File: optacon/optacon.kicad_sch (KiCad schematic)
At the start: 5 parts

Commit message: driver board
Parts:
- added C5: 0.1µF, Capacitor_SMD:C_1206_3216Metric, symbol Device:C
- added R7: 0R, Resistor_SMD:R_1206_3216Metric, symbol Device:R
- added R8: DNP, Resistor_SMD:R_1206_3216Metric, symbol Device:R
- D1: value (none) -> D; footprint (none) -> Diode_SMD:D_SOD-123F
- J1: value (none) -> Conn_01x12; footprint (none) -> microchip_hv:FH34SRJ-12S-0.5SH
- U1, U2: value (none) -> HV528; footprint (none) -> Package_DFN_QFN:HVQFN-32-1EP_5x5mm_P0.5mm_EP3.1x3.1mm
- piezo1: value (none) -> Conn_01x21; footprint (none) -> microchip_hv:piezox20
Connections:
- net AIN: now also J1.2 (Pin_2); no longer J1.11 (Pin_11)
- net CLK: now also J1.10 (Pin_10); no longer J1.4 (Pin_4)
- net DIN: now also J1.11 (Pin_11), U2.17 (DIN); no longer J1.3 (Pin_3), U1.17 (DIN)
- net DOUT: now also U1.24 (DOUT); no longer U2.24 (DOUT)
- net GND: now also J1.1 (Pin_1), C5.1; no longer J1.12 (Pin_12)
- net LE: now also J1.8 (Pin_8); no longer J1.6 (Pin_6)
- net POL: now also J1.9 (Pin_9); no longer J1.5 (Pin_5)
- net REG: now also J1.3 (Pin_3); no longer J1.10 (Pin_10)
- net SCL: now also J1.5 (Pin_5); no longer J1.8 (Pin_8)
- net SDA: now also J1.4 (Pin_4); no longer J1.9 (Pin_9)
- net VBIAS: now also J1.6 (Pin_6); no longer J1.2 (Pin_2)
- net VDD: now also J1.12 (Pin_12); no longer J1.1 (Pin_1)
- net VPP: now also C5.2, R7.2, R8.2
- new net: U1.17 (DIN), U2.24 (DOUT)
- new net VBST: R8.1
- new net VOUT: R7.1
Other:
- sheet hv_driver ports: added VBST; removed none
- moved on the sheet: J1

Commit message: cleanup
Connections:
- net AIN: now also J1.8 (Pin_8); no longer J1.2 (Pin_2)
- net CLK: now also J1.6 (Pin_6); no longer J1.10 (Pin_10)
- net DIN: now also J1.7 (Pin_7); no longer J1.11 (Pin_11)
- net DOUT: now also J1.3 (Pin_3); no longer J1.7 (Pin_7)
- net LE: now also J1.4 (Pin_4); no longer J1.8 (Pin_8)
- net POL: now also J1.5 (Pin_5); no longer J1.9 (Pin_9)
- net REG: now also J1.11 (Pin_11); no longer J1.3 (Pin_3)
- net SCL: now also J1.9 (Pin_9); no longer J1.5 (Pin_5)
- net SDA: now also J1.10 (Pin_10); no longer J1.4 (Pin_4)
- net VBIAS: now also J1.2 (Pin_2); no longer J1.6 (Pin_6)
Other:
- moved on the sheet: R7, R8
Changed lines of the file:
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@@
   (junction (at 167.64 43.18) (diameter 0) (color 0 0 0 0)
   )
+  (junction (at 111.76 92.71) (diameter 0) (color 0 0 0 0)
+  )
   (junction (at 214.63 113.03) (diameter 0) (color 0 0 0 0)
   )
@@
   )
   (junction (at 214.63 66.04) (diameter 0) (color 0 0 0 0)
-  )
-  (junction (at 111.76 92.71) (diameter 0) (color 0 0 0 0)
   )
   (junction (at 214.63 68.58) (diameter 0) (color 0 0 0 0)
@@
     (stroke (width 0) (type default) (color 0 0 0 0))
   )
-  (wire (pts (xy 104.14 97.79) (xy 104.14 99.06))
-    (stroke (width 0) (type default) (color 0 0 0 0))
-  )
   (wire (pts (xy 214.63 110.49) (xy 214.63 111.76))
     (stroke (width 0) (type default) (color 0 0 0 0))
@@
     (stroke (width 0) (type default) (color 0 0 0 0))
   )
+  (wire (pts (xy 54.61 91.44) (xy 59.69 91.44))
+    (stroke (width 0) (type default) (color 0 0 0 0))
+  )
   (wire (pts (xy 210.82 115.57) (xy 214.63 115.57))
     (stroke (width 0) (type default) (color 0 0 0 0))
@@
     (stroke (width 0) (type default) (color 0 0 0 0))
   )
-  (wire (pts (xy 111.76 92.71) (xy 111.76 99.06))
+  (wire (pts (xy 111.76 92.71) (xy 111.76 97.79))
     (stroke (width 0) (type default) (color 0 0 0 0))
   )
@@
     (stroke (width 0) (type default) (color 0 0 0 0))
   )
+  (wire (pts (xy 111.76 87.63) (xy 111.76 92.71))
+    (stroke (width 0) (type default) (color 0 0 0 0))
+  )
   (wire (pts (xy 210.82 73.66) (xy 214.63 73.66))
     (stroke (width 0) (type default) (color 0 0 0 0))
@@
     (stroke (width 0) (type default) (color 0 0 0 0))
   )
-  (wire (pts (xy 104.14 87.63) (xy 104.14 92.71))
-    (stroke (width 0) (type default) (color 0 0 0 0))
-  )
   (wire (pts (xy 168.91 40.64) (xy 168.91 107.95))
     (stroke (width 0) (type default) (color 0 0 0 0))
@@
     (effects (font (size 1.27 1.27)) (justify right bottom))
   )
-  (label "AIN" (at 27.94 66.04 0)
+  (label "AIN" (at 27.94 50.8 0)
     (effects (font (size 1.27 1.27)) (justify left bottom))
   )
@@
     (effects (font (size 1.27 1.27)) (justify right bottom))
   )
-  (label "DOUT" (at 27.94 53.34 0)
+  (label "DOUT" (at 27.94 63.5 0)
     (effects (font (size 1.27 1.27)) (justify left bottom))
   )
@@
     (effects (font (size 1.27 1.27)) (justify left bottom))
   )
-  (label "SDA" (at 27.94 60.96 0)
+  (label "SDA" (at 27.94 45.72 0)
     (effects (font (size 1.27 1.27)) (justify left bottom))
   )
@@
     (effects (font (size 1.27 1.27)) (justify left bottom))
   )
-  (label "DIN" (at 27.94 43.18 0)
+  (label "DIN" (at 27.94 53.34 0)
     (effects (font (size 1.27 1.27)) (justify left bottom))
   )
@@
     (effects (font (size 1.27 1.27)) (justify left bottom))
   )
-  (label "POL" (at 27.94 48.26 0)
+  (label "POL" (at 27.94 58.42 0)
     (effects (font (size 1.27 1.27)) (justify left bottom))
   )
@@
     (effects (font (size 1.27 1.27)) (justify left bottom))
   )
-  (label "LE" (at 27.94 50.8 0)
+  (label "LE" (at 27.94 60.96 0)
     (effects (font (size 1.27 1.27)) (justify left bottom))
   )
@@
     (effects (font (size 1.27 1.27)) (justify left bottom))
   )
-  (label "VBIAS" (at 27.94 55.88 0)
+  (label "VBIAS" (at 27.94 66.04 0)
     (effects (font (size 1.27 1.27)) (justify left bottom))
   )
@@
     (effects (font (size 1.27 1.27)) (justify left bottom))
   )
-  (label "CLK" (at 27.94 45.72 0)
-    (effects (font (size 1.27 1.27)) (justify left bottom))
-  )
-  (label "REG" (at 27.94 63.5 0)
+  (label "CLK" (at 27.94 55.88 0)
+    (effects (font (size 1.27 1.27)) (justify left bottom))
+  )
+  (label "REG" (at 27.94 43.18 0)
     (effects (font (size 1.27 1.27)) (justify left bottom))
   )
@@
     (effects (font (size 1.27 1.27)) (justify right bottom))
   )
-  (label "SCL" (at 27.94 58.42 0)
+  (label "SCL" (at 27.94 48.26 0)
     (effects (font (size 1.27 1.27)) (justify left bottom))
   )
@@
     (pin "1")
   )
-  (symbol (lib_id "Device:R") (at 107.95 92.71 90) (unit 1)
-    (in_bom yes) (on_board yes) (fields_autoplaced)
-    (property "Reference" "R7" (id 0) (at 107.95 86.36 90))
-    (property "Value" "0R" (id 1) (at 107.95 88.9 90))
-    (property "Footprint" "Resistor_SMD:R_1206_3216Metric" (id 2) (at 107.95 94.488 90)
-      (effects (font (size 1.27 1.27)) hide)
-    )
-    (property "Datasheet" "~" (id 3) (at 107.95 92.71 0)
+  (symbol (lib_id "Device:R") (at 107.95 87.63 90) (unit 1)
+    (in_bom yes) (on_board yes) (fields_autoplaced)
+    (property "Reference" "R7" (id 0) (at 107.95 81.28 90))
+    (property "Value" "0R" (id 1) (at 107.95 83.82 90))
+    (property "Footprint" "Resistor_SMD:R_1206_3216Metric" (id 2) (at 107.95 89.408 90)
+      (effects (font (size 1.27 1.27)) hide)
+    )
+    (property "Datasheet" "~" (id 3) (at 107.95 87.63 0)
       (effects (font (size 1.27 1.27)) hide)
     )
@@
     (pin "1")
   )
-  (symbol (lib_id "Device:R") (at 107.95 99.06 90) (unit 1)
+  (symbol (lib_id "power:GND") (at 54.61 91.44 0) (unit 1)
+    (in_bom yes) (on_board yes) (fields_autoplaced)
+    (property "Reference" "#PWR0109" (id 0) (at 54.61 97.79 0)
+      (effects (font (size 1.27 1.27)) hide)
+    )
+    (property "Value" "GND" (id 1) (at 54.61 96.52 0))
+    (property "Footprint" "" (id 2) (at 54.61 91.44 0)
+      (effects (font (size 1.27 1.27)) hide)
+    )
+    (property "Datasheet" "" (id 3) (at 54.61 91.44 0)
+      (effects (font (size 1.27 1.27)) hide)
+    )
+    (pin "1")
+  )
+  (symbol (lib_id "Device:R") (at 107.95 97.79 90) (unit 1)
     (in_bom yes) (on_board yes)
-    (property "Reference" "R8" (id 0) (at 107.95 101.6 90))
-    (property "Value" "DNP" (id 1) (at 107.95 104.14 90))
-    (property "Footprint" "Resistor_SMD:R_1206_3216Metric" (id 2) (at 107.95 100.838 90)
-      (effects (font (size 1.27 1.27)) hide)
-    )
-    (property "Datasheet" "~" (id 3) (at 107.95 99.06 0)
+    (property "Reference" "R8" (id 0) (at 107.95 100.33 90))
+    (property "Value" "DNP" (id 1) (at 107.95 102.87 90))
+    (property "Footprint" "Resistor_SMD:R_1206_3216Metric" (id 2) (at 107.95 99.568 90)
+      (effects (font (size 1.27 1.27)) hide)
+    )
+    (property "Datasheet" "~" (id 3) (at 107.95 97.79 0)
       (effects (font (size 1.27 1.27)) hide)
     )
@@
       (effects (font (size 1.27 1.27)) (justify right))
     )
-    (pin "IN-" input (at 59.69 90.17 180)
+    (pin "IN-" input (at 59.69 91.44 180)
       (effects (font (size 1.27 1.27)) (justify left))
     )
@@
       (effects (font (size 1.27 1.27)) (justify left))
     )
-    (pin "VBST" input (at 80.01 97.79 0)
+    (pin "VBST" output (at 80.01 97.79 0)
       (effects (font (size 1.27 1.27)) (justify right))
     )
@@
       (reference "#PWR0108") (unit 1) (value "GND") (footprint "")
     )
+    (path "/bd9366dd-55fd-4568-ac76-a24a9da5118d"
+      (reference "#PWR0109") (unit 1) (value "GND") (footprint "")
+    )
     (path "/de858789-f791-428c-b810-2c6120320e8e/7b4fcf13-8465-4e87-8365-1371db28d783"

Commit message: gerbers
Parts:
- C5: value 0.1µF -> 0.1µF 150V+; Part (none) -> C76671
- R7: Part (none) -> C108081
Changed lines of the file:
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@@
+      (effects (font (size 1.27 1.27)) hide)
+    )
+    (property "Part" "C108081" (id 4) (at 107.95 87.63 0)
       (effects (font (size 1.27 1.27)) hide)
     )
@@
       (effects (font (size 1.27 1.27)) (justify right))
     )
-    (property "Value" "0.1µF" (id 1) (at 123.19 97.7899 0)
+    (property "Value" "0.1µF 150V+" (id 1) (at 123.19 97.7899 0)
       (effects (font (size 1.27 1.27)) (justify right))
     )
@@
     )
     (property "Datasheet" "~" (id 3) (at 119.38 96.52 0)
+      (effects (font (size 1.27 1.27)) hide)
+    )
+    (property "Part" "C76671" (id 4) (at 119.38 96.52 0)
       (effects (font (size 1.27 1.27)) hide)
     )
@@
     )
     (path "/e675c196-c205-4a25-8e1c-e666c9b3d5ee"
-      (reference "C5") (unit 1) (value "0.1µF") (footprint "Capacitor_SMD:C_1206_3216Metric")
+      (reference "C5") (unit 1) (value "0.1µF 150V+") (footprint "Capacitor_SMD:C_1206_3216Metric")
     )
     (path "/94d5cf93-1182-4470-86cd-c981a2884463"
@@
     )
     (path "/de858789-f791-428c-b810-2c6120320e8e/22e21f68-cd84-41eb-a5bd-60af16052ef5"
-      (reference "R6") (unit 1) (value "0") (footprint "Resistor_SMD:R_0603_1608Metric")
+      (reference "R6") (unit 1) (value "DNP") (footprint "Resistor_SMD:R_0603_1608Metric")
     )
     (path "/4a94f1af-dee9-45e1-8f3c-805cbdb3c8ac"

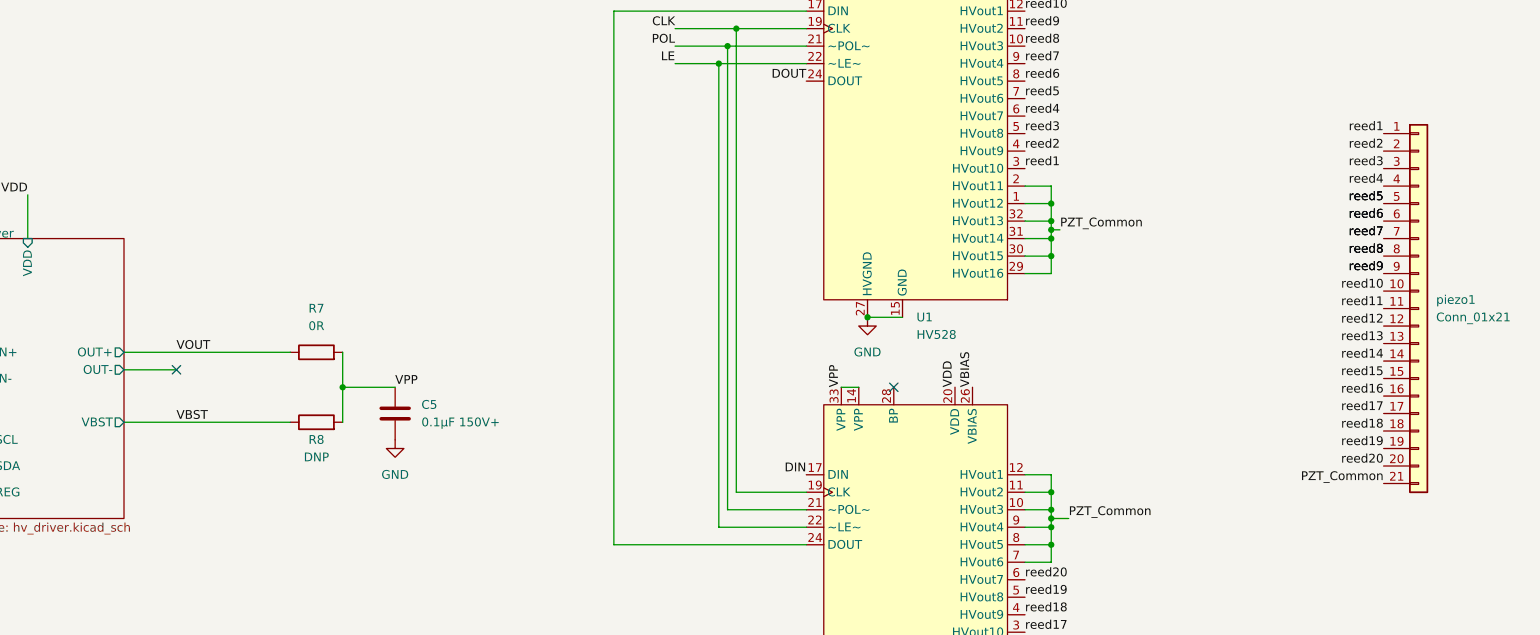
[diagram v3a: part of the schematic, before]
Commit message: WIP -added clearance for reeds center conductor header pins -removed jumper resistor & output cap on VBST -changed C4 high voltage cap to 0805, lower height above board -added C5 10µF cap at inductor -changed hole pattern on piezo to PTH for smaller holes -added copper fill under piezo for equal height -removed alignment holes around piezo, replaced with front silkscreen alignment arrows -reworked layout on DRV2665 a bit according to datasheet guidelines -moved fpc connector to top
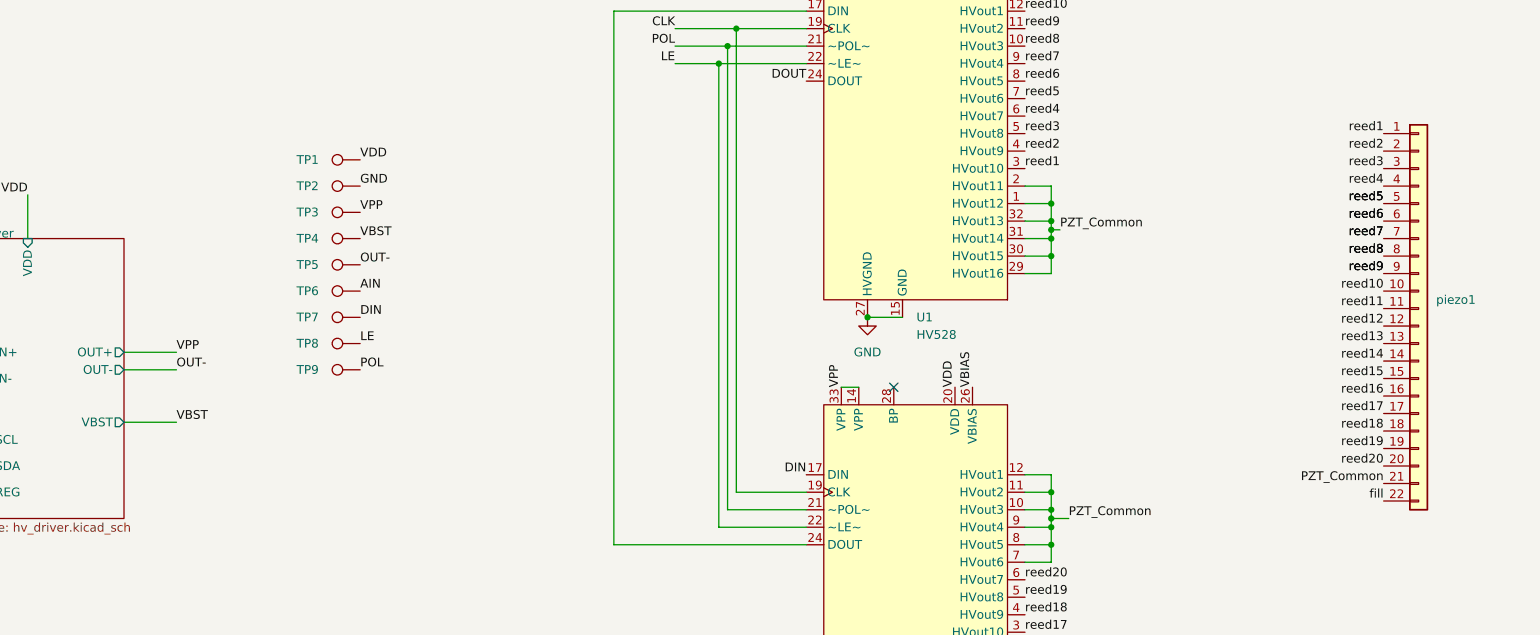
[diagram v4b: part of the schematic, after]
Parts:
- removed C5: 0.1µF 150V+, Capacitor_SMD:C_1206_3216Metric, symbol Device:C
- removed R7: 0R, Resistor_SMD:R_1206_3216Metric, symbol Device:R
- removed R8: DNP, Resistor_SMD:R_1206_3216Metric, symbol Device:R
- added TP1, TP2, TP3, TP4, TP5, TP6, TP7, TP8, TP9: TestPoint, TestPoint:TestPoint_Pad_D1.5mm, symbol Connector:TestPoint
- piezo1: value Conn_01x21 -> Conn_01x22; symbol Connector_Generic:Conn_01x21 -> Connector_Generic:Conn_01x22
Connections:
- net AIN: now also TP6.1
- net DIN: now also TP7.1
- net GND: now also TP2.1
- net LE: now also TP8.1
- net POL: now also TP9.1
- net VBST: now also TP4.1
- net VDD: now also TP1.1
- net VPP: now also TP3.1
- new net OUT-: TP5.1
- new net fill: piezo1.22 (Pin_22)
- no-connect marks 3 -> 2

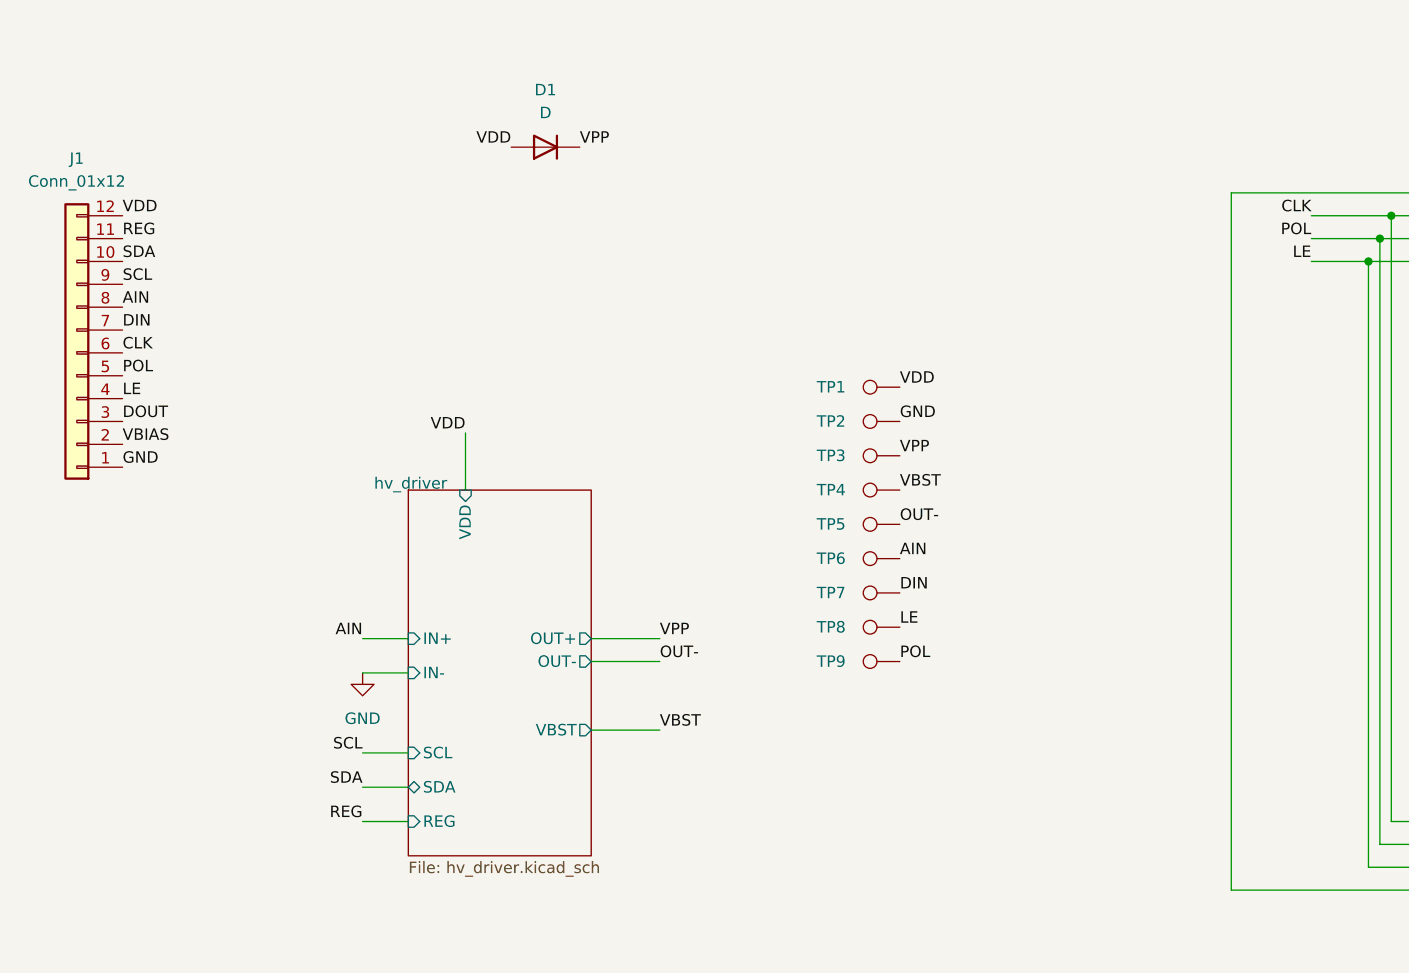
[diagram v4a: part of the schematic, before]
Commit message: add test points, mounting holes
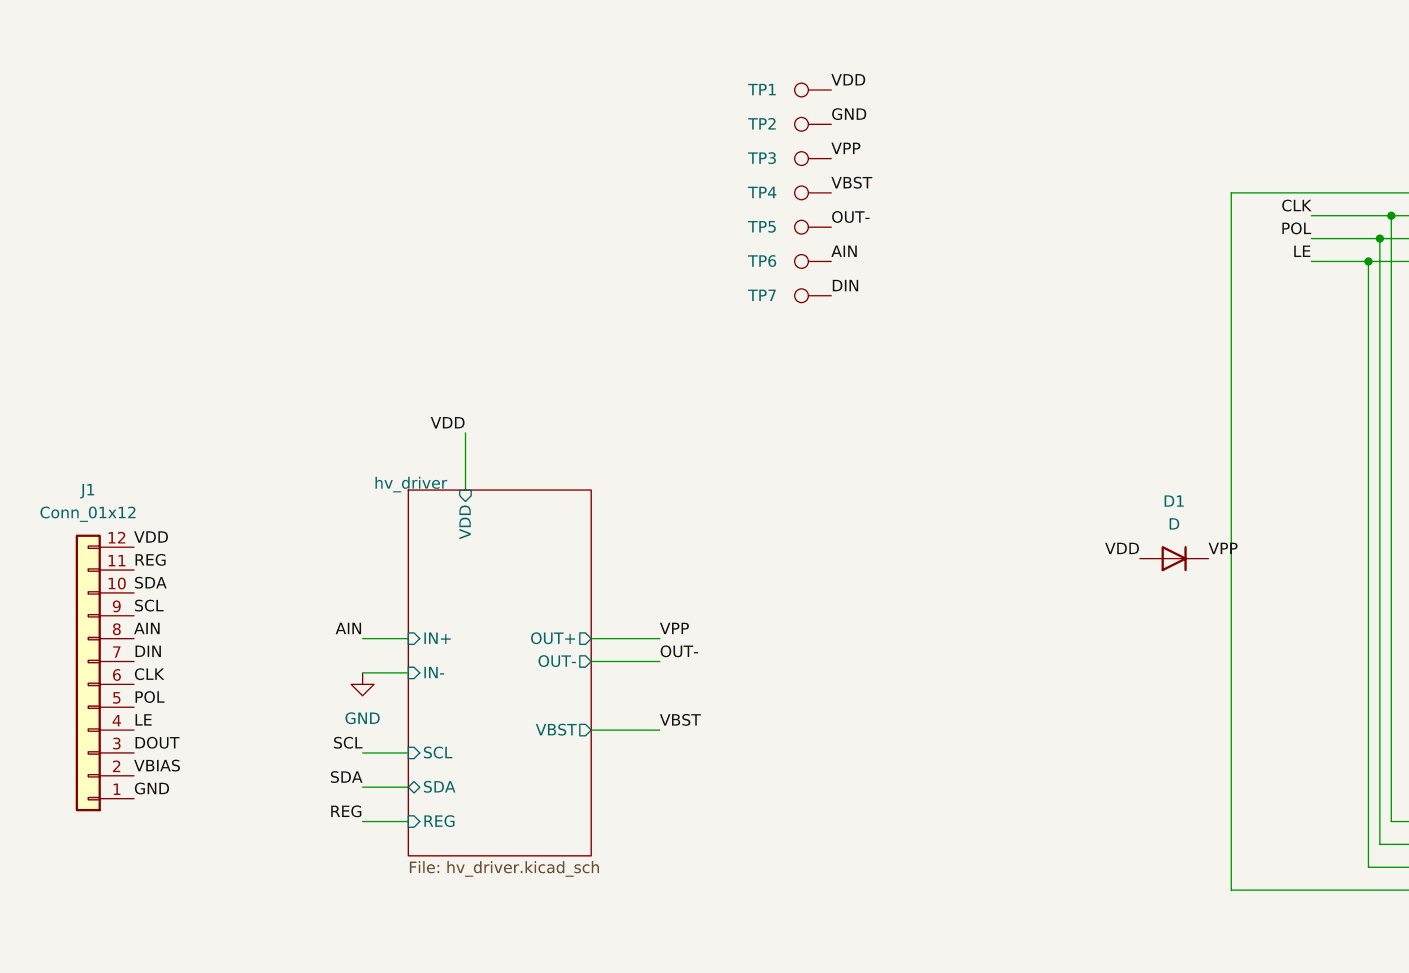
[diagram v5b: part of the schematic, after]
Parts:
- removed TP8, TP9: TestPoint, TestPoint:TestPoint_Pad_D1.5mm, symbol Connector:TestPoint
- TP1, TP2, TP3, TP4, TP5, TP6, TP7: footprint TestPoint:TestPoint_Pad_D1.5mm -> TestPoint:TestPoint_Pad_D1.0mm
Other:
- moved on the sheet: D1, J1, TP1, TP2, TP3, TP4, TP5, TP6, TP7
